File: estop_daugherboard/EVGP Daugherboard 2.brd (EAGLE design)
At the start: 82.6 x 94.1 mm, 41 parts, among them J1 JST-XH-02-PIN-LONG-PAD, J2 JST-XH-02-PIN-LONG-PAD, J3 JST-XH-03-PIN-LONG-PAD, J4 JST-XH-03-PIN-LONG-PAD, J5 AVR_SPI_PROG_3X2PTH, J6 UX60-MB-5S8, J7 4_XH_JST, Q1 N_FET2, Q2 N_FET1, U1 NL27WZ08USG, U2 ATMEGA32U4-AU, X1 TSX-3225 16.0000MF18X-AC0

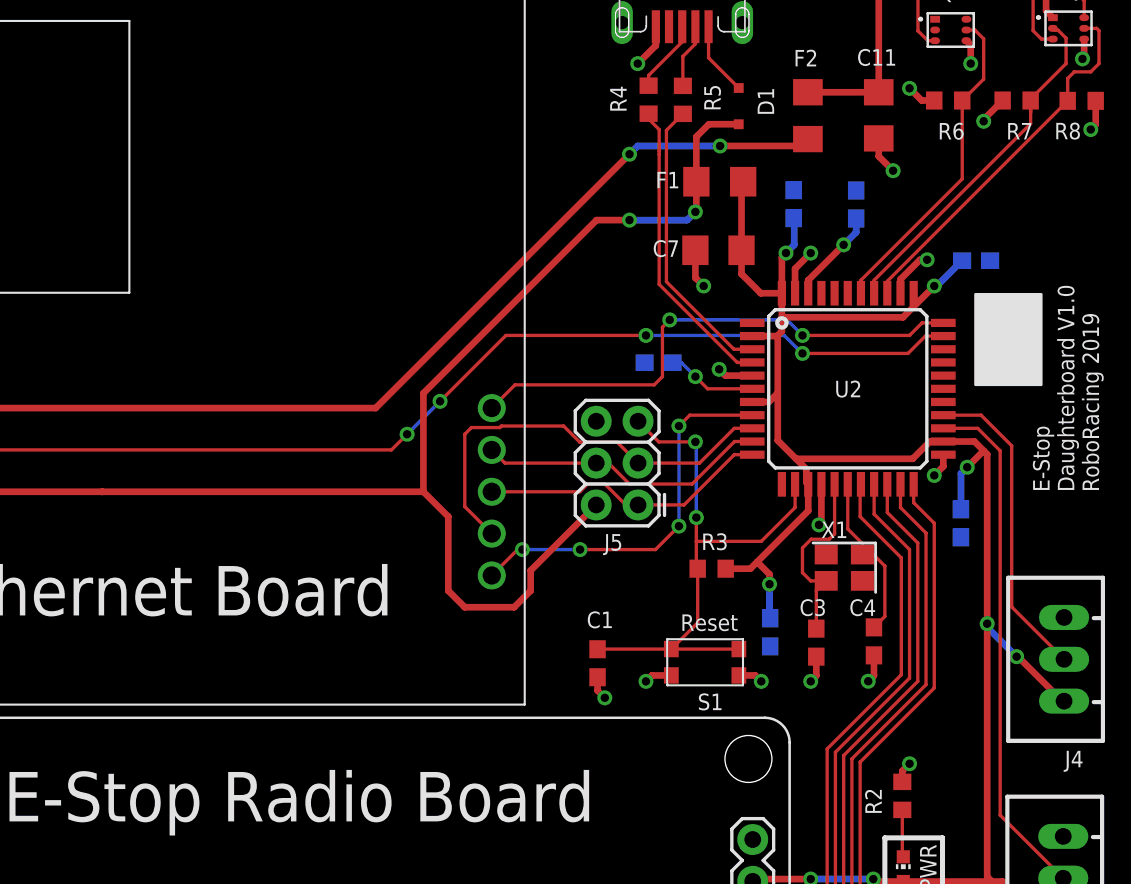
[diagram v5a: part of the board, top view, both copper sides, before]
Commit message: fixed drc errors
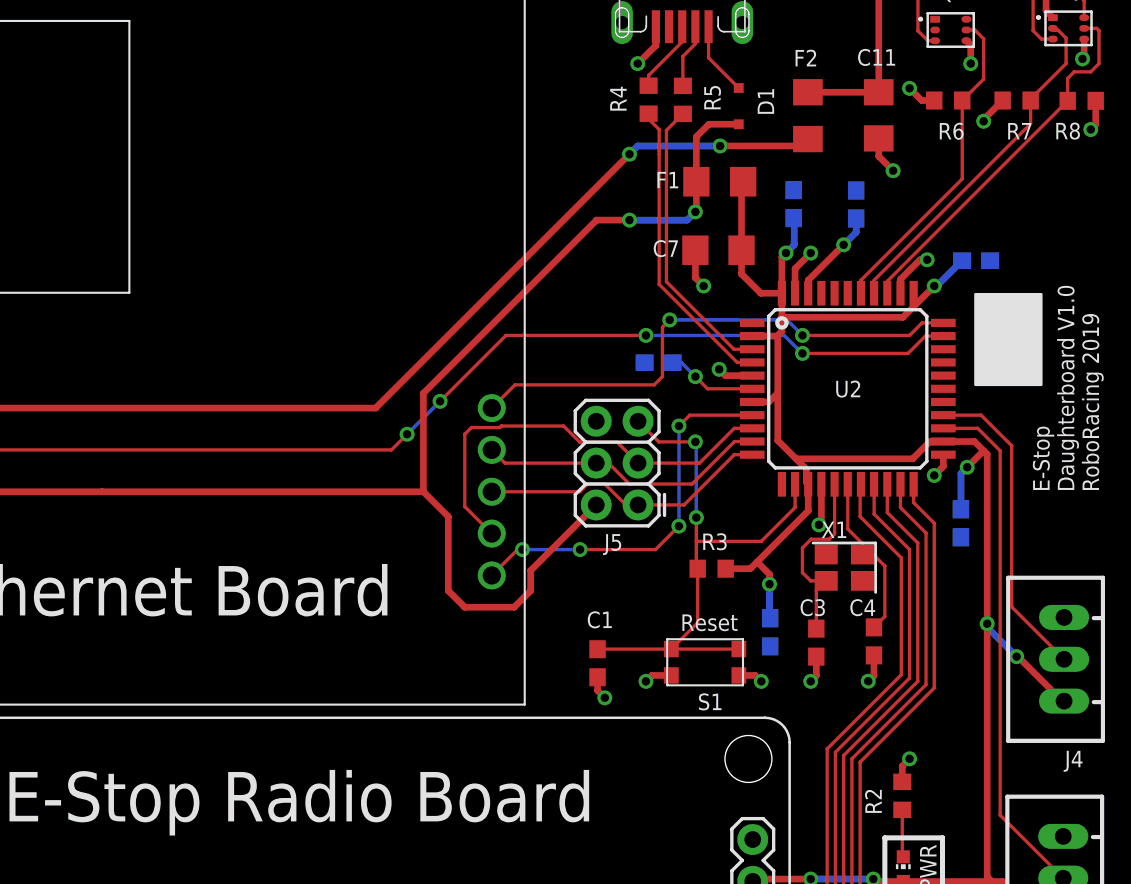
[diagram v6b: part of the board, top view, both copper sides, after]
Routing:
- net STACK_MCU2: track 22.1 -> 21.4 mm
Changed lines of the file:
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@@
 <wire x1="72.84" y1="38.85355625" x2="72.493221875" y2="38.506778125" width="0.4064" layer="1"/>
 <via x="72.493221875" y="38.506778125" extent="1-16" drill="0.508"/>
-<wire x1="74.56" y1="32.4" x2="74.56" y2="33.06" width="0.4064" layer="1"/>
-<wire x1="74.56" y1="33.06" x2="75" y2="33.5" width="0.4064" layer="1"/>
-<via x="75" y="33.5" extent="1-16" drill="0.508"/>
+<wire x1="74.56" y1="32.4" x2="74.56" y2="33.36" width="0.4064" layer="1"/>
+<wire x1="74.56" y1="33.36" x2="75" y2="33.8" width="0.4064" layer="1"/>
+<via x="75" y="33.8" extent="1-16" drill="0.508"/>
 <wire x1="74.74" y1="18.55" x2="74.74" y2="17.26" width="0.4064" layer="1"/>
 <wire x1="74.74" y1="17.26" x2="75" y2="17" width="0.4064" layer="1"/>
@@
 <wire x1="62.058" y1="71.558" x2="62.82" y2="72.32" width="0.4064" layer="1"/>
 <wire x1="9.64" y1="50.01" x2="25.99" y2="50.01" width="0.4064" layer="1"/>
-<wire x1="26" y1="50" x2="25.99" y2="50.01" width="0.4064" layer="1"/>
 <wire x1="45.49" y1="50.01" x2="25.99" y2="50.01" width="0.4064" layer="1"/>
 <wire x1="55.98" y1="49.21" x2="52" y2="45.23" width="0.4064" layer="1"/>
@@
 <wire x1="84.5" y1="76" x2="84.5" y2="77.54395625" width="0.2032" layer="1"/>
 <wire x1="84.5" y1="77.54395625" x2="84.01375625" y2="78.0302" width="0.2032" layer="1"/>
-<wire x1="82.35" y1="73.0325" x2="82.35" y2="73.76" width="0.2032" layer="1"/>
-<wire x1="82.35" y1="73.76" x2="82.35" y2="72.35" width="0.2032" layer="1"/>
 <wire x1="72.85" y1="62.85" x2="72.85" y2="62.06" width="0.2032" layer="1"/>
-<wire x1="82.35" y1="72.35" x2="72.85" y2="62.85" width="0.2032" layer="1"/>
+<wire x1="72.85" y1="62.85" x2="82.35" y2="72.35" width="0.2032" layer="1"/>
+<wire x1="82.35" y1="72.35" x2="82.35" y2="73.76" width="0.2032" layer="1"/>
 </signal>
 <signal name="STACK_MCU3">
